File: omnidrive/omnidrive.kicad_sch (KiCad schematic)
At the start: 43 parts, among them J1 AudioJack3, J2 Conn_01x01_Pin, J3 Conn_01x01_Pin, SW1 SW_SPDT, SW2 SW_SPDT, SW3 SW_SPST, SW4 SW_SPDT, U1 TL072, U2 TL072

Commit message: annotation and ERC check
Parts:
- added C10: 0.1uF, symbol Device:C
- added C11, C8: 1uF, symbol Device:C_Polarized
- added C9: 0.047uF, symbol Device:C
- added J4, J5: Conn_01x01_Pin, symbol Connector:Conn_01x01_Pin
- added J6: AudioJack2, symbol Connector_Audio:AudioJack2
- added R18: 3.9K, symbol Device:R
- added R19: 10K, symbol Device:R
- added R20: 1K, symbol Device:R
- added RV2_Tone1: 10K, symbol Device:R_Potentiometer
- added RV3_BLEND1: 47K Log, symbol Device:R_Potentiometer
- added RV4_VOL1: 100K Log, symbol Device:R_Potentiometer
- added SW5: SW_SPST, symbol Switch:SW_SPST
- renumbered RV1 to RV1_GAIN1
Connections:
- net GND: now also C7.2, C10.1, R19.2, RV4_VOL1.3, SW5.2 (B)
- net at R17.1: now also C6.2, RV1_GAIN1.2, RV1_GAIN1.3, U2.7
- net at R17.2: now also D3.1 (K), D4.2 (A), C8.1, C9.1
- net at D4.1 (K): now also D3.2 (A), SW4.2 (B)
- net at SW4.1 (A): now also C12.1
- net at SW4.3 (C): now also C6.1, R16.1, RV1_GAIN1.1, U2.6 (-)
- net at R16.2: now also C7.1
- net at SW2.3 (C): now also C11.1
- new net: C11.2, RV3_BLEND1.3
- new net: C8.2, R18.2
- new net: C9.2, R19.1, R20.1, RV2_Tone1.3
- new net: C10.2, R18.1, RV2_Tone1.1
- new net: RV3_BLEND1.2, RV4_VOL1.1
- new net: J5.1 (Pin_1), J6.T, RV4_VOL1.2
- new net: R20.2, SW5.1 (A)
- new net: RV2_Tone1.2, RV3_BLEND1.1
- new net: J4.1 (Pin_1), J6.S

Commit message: offboarding
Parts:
- added J_BLEND_1, J_BLEND_2, J_BLEND_3, J_BOOST_1, J_BOOST_2, J_BOOST_3, J_FILT_1, J_FILT_2, J_FILT_3, J_GAIN_1, J_GAIN_2, J_GAIN_3, J_MODE_1, J_MODE_2, J_MODE_3, J_OCT_1, J_OCT_2, J_SCOOP_1, J_SCOOP_2, J_TONE_1, J_TONE_2, J_TONE_3, J_VOL_1, J_VOL_2, J_VOL_3: Conn_01x01_Pin, symbol Connector:Conn_01x01_Pin
- renumbered J2 to J_IN_SLV1, J3 to J_IN_TIP1, J4 to J_OUT_SLV1, J5 to J_OUT_TIP1, SW1 to SW_BOOST_1, SW2 to SW_FILTER_2, SW4 to SW_MODE1, SW3 to SW_OCTAVE1, SW5 to SW_SCOOP1
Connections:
- net GND: now also J1.S, J_IN_SLV1.1 (Pin_1), J_SCOOP_1.1 (Pin_1), J_VOL_1.1 (Pin_1)
- net at C11.1, SW_FILTER_2.3 (C): now also J_FILT_2.1 (Pin_1)
- net at C11.2, RV3_BLEND1.3: now also J_BLEND_1.1 (Pin_1)
- net at C6.2, R17.1, RV1_GAIN1.2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: now also J_GAIN_2.1 (Pin_1), J_GAIN_3.1 (Pin_1)
- net at R10.2, R11.2, SW_FILTER_2.2 (B): now also J_FILT_3.1 (Pin_1)
- net at D3.2 (A), D4.1 (K), SW_MODE1.2 (B): now also J_MODE_3.1 (Pin_1)
- net at C9.2, R19.1, R20.1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: now also J_TONE_2.1 (Pin_1)
- net at C10.2, R18.1, RV2_Tone1.1: now also J_TONE_1.1 (Pin_1)
- net at C1.1, R1.1, SW_BOOST_1.3 (C): now also J_BOOST_2.1 (Pin_1)
- net at RV3_BLEND1.2, RV4_VOL1.1: now also J_BLEND_2.1 (Pin_1), J_VOL_3.1 (Pin_1)
- net at J6.T, J_OUT_TIP1.1 (Pin_1), RV4_VOL1.2: now also J_VOL_2.1 (Pin_1)
- net at C12.1, SW_MODE1.1 (A): now also J_MODE_2.1 (Pin_1)
- net at C6.1, R16.1, RV1_GAIN1.1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: now also J_GAIN_1.1 (Pin_1), J_MODE_1.1 (Pin_1)
- net at D1.2 (A), R12.2, U2.2 (-): now also R11.1
- net at J1.T, J_IN_TIP1.1 (Pin_1), SW_BOOST_1.2 (B): now also J_BOOST_1.1 (Pin_1)
- net at R13.2, R14.2, SW_OCTAVE1.1 (A): now also J_OCT_2.1 (Pin_1)
- net at C2.1, R2.1, SW_BOOST_1.1 (A): now also J_BOOST_3.1 (Pin_1)
- net at R20.2, SW_SCOOP1.1 (A): now also J_SCOOP_2.1 (Pin_1)
- net at RV2_Tone1.2, RV3_BLEND1.1: now also J_BLEND_3.1 (Pin_1), J_TONE_3.1 (Pin_1)
- net at R9.1, SW_FILTER_2.1 (A), U1.7: now also J_FILT_1.1 (Pin_1)

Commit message: assigned footprints
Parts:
- C1, C2, C3, C4, C5, C6, C9: footprint (none) -> Capacitor_SMD:C_1206_3216Metric_Pad1.33x1.80mm_HandSolder
- C10: footprint (none) -> Capacitor_THT:C_Rect_L11.0mm_W6.3mm_P10.00mm_MKT
- C11, C8, J6: footprint (none) -> Capacitor_THT:CP_Radial_D6.3mm_P2.50mm
- C12, C13, C14, C7: footprint (none) -> Capacitor_THT:CP_Radial_D5.0mm_P2.50mm
- J_BLEND_1, J_BLEND_2, J_BLEND_3, J_BOOST_1, J_BOOST_2, J_BOOST_3, J_FILT_1, J_FILT_2, J_FILT_3, J_GAIN_1, J_GAIN_2, J_GAIN_3, J_IN_SLV1, J_IN_TIP1, J_MODE_1, J_MODE_2, J_MODE_3, J_OCT_1, J_OCT_2, J_OUT_SLV1, J_OUT_TIP1, J_SCOOP_1, J_SCOOP_2, J_TONE_1, J_TONE_2, J_TONE_3, J_VOL_1, J_VOL_2, J_VOL_3: footprint (none) -> Connector_PinHeader_1.00mm:PinHeader_1x01_P1.00mm_Vertical
- R1, R10, R11, R12, R13, R14, R15, R16, R17, R18, R19, R2, R20, R21, R22, R3, R4, R5, R6, R7, R8, R9, U1, U2: footprint (none) -> Resistor_SMD:R_1206_3216Metric_Pad1.30x1.75mm_HandSolder

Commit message: start placement
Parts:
- added BT1: 9V, symbol Device:Battery_Cell
- added J_BATT_NEG1, J_BATT_POS1: Conn_01x01_Pin, Connector_PinHeader_1.00mm:PinHeader_1x01_P1.00mm_Vertical, symbol Connector:Conn_01x01_Pin
- U1, U2: footprint Resistor_SMD:R_1206_3216Metric_Pad1.30x1.75mm_HandSolder -> Package_DIP:DIP-8_W7.62mm
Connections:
- net +9V: now also BT1.1 (+), J_BATT_POS1.1 (Pin_1)
- net at J1.R: now also BT1.2 (-), J_BATT_NEG1.1 (Pin_1)
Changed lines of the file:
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@@
   (junction (at 67.31 25.4) (diameter 0) (color 0 0 0 0)
   )
+  (junction (at 35.56 67.31) (diameter 0) (color 0 0 0 0)
+  )
+  (junction (at 60.96 63.5) (diameter 0) (color 0 0 0 0)
+  )
   (junction (at 97.79 77.47) (diameter 0) (color 0 0 0 0)
   )
@@
   (junction (at 76.2 77.47) (diameter 0) (color 0 0 0 0)
   )
+  (junction (at 22.86 48.26) (diameter 0) (color 0 0 0 0)
+  )
   (junction (at 191.77 114.3) (diameter 0) (color 0 0 0 0)
   )
@@
   (junction (at 135.89 36.83) (diameter 0) (color 0 0 0 0)
   )
+  (junction (at 35.56 58.42) (diameter 0) (color 0 0 0 0)
+  )
   (junction (at 64.77 63.5) (diameter 0) (color 0 0 0 0)
   )
@@
     (stroke (width 0) (type default))
   )
+  (wire (pts (xy 45.72 58.42) (xy 60.96 58.42))
+    (stroke (width 0) (type default))
+  )
   (wire (pts (xy 170.18 53.34) (xy 170.18 55.88))
     (stroke (width 0) (type default))
@@
     (stroke (width 0) (type default))
   )
+  (wire (pts (xy 20.32 58.42) (xy 35.56 58.42))
+    (stroke (width 0) (type default))
+  )
   (wire (pts (xy 255.27 16.51) (xy 255.27 67.31))
     (stroke (width 0) (type default))
@@
     (stroke (width 0) (type default))
   )
+  (wire (pts (xy 31.75 33.02) (xy 31.75 40.64))
+    (stroke (width 0) (type default))
+  )
   (wire (pts (xy 128.27 101.6) (xy 128.27 67.31))
     (stroke (width 0) (type default))
@@
     (stroke (width 0) (type default))
   )
+  (wire (pts (xy 60.96 58.42) (xy 60.96 63.5))
+    (stroke (width 0) (type default))
+  )
   (wire (pts (xy 208.28 35.56) (xy 204.47 35.56))
     (stroke (width 0) (type default))
@@
     (stroke (width 0) (type default))
   )
+  (wire (pts (xy 31.75 40.64) (xy 22.86 40.64))
+    (stroke (width 0) (type default))
+  )
   (wire (pts (xy 191.77 99.06) (xy 191.77 101.6))
     (stroke (width 0) (type default))
   )
-  (wire (pts (xy 55.88 63.5) (xy 64.77 63.5))
+  (wire (pts (xy 55.88 63.5) (xy 60.96 63.5))
     (stroke (width 0) (type default))
   )
@@
     (stroke (width 0) (type default))
   )
+  (wire (pts (xy 22.86 48.26) (xy 20.32 48.26))
+    (stroke (width 0) (type default))
+  )
   (wire (pts (xy 80.01 36.83) (xy 85.09 36.83))
     (stroke (width 0) (type default))
@@
     (stroke (width 0) (type default))
   )
+  (wire (pts (xy 35.56 67.31) (xy 45.72 67.31))
+    (stroke (width 0) (type default))
+  )
   (wire (pts (xy 148.59 36.83) (xy 156.21 36.83))
     (stroke (width 0) (type default))
@@
     (stroke (width 0) (type default))
   )
+  (wire (pts (xy 35.56 58.42) (xy 35.56 67.31))
+    (stroke (width 0) (type default))
+  )
   (wire (pts (xy 144.78 93.98) (xy 144.78 101.6))
     (stroke (width 0) (type default))
@@
     (stroke (width 0) (type default))
   )
+  (wire (pts (xy 22.86 40.64) (xy 22.86 48.26))
+    (stroke (width 0) (type default))
+  )
   (wire (pts (xy 134.62 20.32) (xy 142.24 20.32))
     (stroke (width 0) (type default))
@@
     (stroke (width 0) (type default))
   )
+  (wire (pts (xy 60.96 63.5) (xy 64.77 63.5))
+    (stroke (width 0) (type default))
+  )
   (wire (pts (xy 187.96 97.79) (xy 187.96 99.06))
     (stroke (width 0) (type default))
@@
     (stroke (width 0) (type default))
   )
+  (wire (pts (xy 45.72 67.31) (xy 45.72 58.42))
+    (stroke (width 0) (type default))
+  )
   (wire (pts (xy 154.94 58.42) (xy 76.2 58.42))
     (stroke (width 0) (type default))
@@
     (stroke (width 0) (type default))
   )
+  (wire (pts (xy 26.67 33.02) (xy 31.75 33.02))
+    (stroke (width 0) (type default))
+  )
   (wire (pts (xy 237.49 25.4) (xy 237.49 30.48))
     (stroke (width 0) (type default))
@@
     (stroke (width 0) (type default))
   )
+  (wire (pts (xy 35.56 58.42) (xy 36.83 58.42))
+    (stroke (width 0) (type default))
+  )
   (wire (pts (xy 64.77 30.48) (xy 69.85 30.48))
     (stroke (width 0) (type default))
@@
     (stroke (width 0) (type default))
   )
+  (wire (pts (xy 20.32 48.26) (xy 20.32 50.8))
+    (stroke (width 0) (type default))
+  )
   (wire (pts (xy 53.34 29.21) (xy 53.34 27.94))
     (stroke (width 0) (type default))
@@
     )
   )
+  (symbol (lib_id "Connector:Conn_01x01_Pin") (at 27.94 48.26 0) (mirror y) (unit 1)
+    (in_bom yes) (on_board yes) (dnp no)
+    (property "Reference" "J_BATT_NEG1" (at 27.305 43.18 0)
+      (effects (font (size 1.27 1.27)))
+    )
+    (property "Value" "Conn_01x01_Pin" (at 27.305 45.72 0)
+      (effects (font (size 1.27 1.27)))
+    )
+    (property "Footprint" "Connector_PinHeader_1.00mm:PinHeader_1x01_P1.00mm_Vertical" (at 27.94 48.26 0)
+      (effects (font (size 1.27 1.27)) hide)
+    )
+    (property "Datasheet" "~" (at 27.94 48.26 0)
+      (effects (font (size 1.27 1.27)) hide)
+    )
+    (pin "1")
+    (instances
+      (project "omnidrive"
+        (path "/2afaead6-7d3e-4c2a-adc8-ba736ff6308b"
+          (reference "J_BATT_NEG1") (unit 1)
+        )
+      )
+    )
+  )
   (symbol (lib_id "power:GND") (at 161.29 114.3 0) (unit 1)
     (in_bom yes) (on_board yes) (dnp no) (fields_autoplaced)
@@
       (effects (font (size 1.27 1.27)))
     )
-    (property "Footprint" "Resistor_SMD:R_1206_3216Metric_Pad1.30x1.75mm_HandSolder" (at 214.63 53.34 0)
+    (property "Footprint" "Package_DIP:DIP-8_W7.62mm" (at 214.63 53.34 0)
       (effects (font (size 1.27 1.27)) hide)
     )
@@
       (effects (font (size 1.27 1.27)))
     )
-    (property "Footprint" "Resistor_SMD:R_1206_3216Metric_Pad1.30x1.75mm_HandSolder" (at 218.44 60.96 0)
+    (property "Footprint" "Package_DIP:DIP-8_W7.62mm" (at 218.44 60.96 0)
       (effects (font (size 1.27 1.27)) hide)
     )
@@
     )
   )
+  (symbol (lib_id "Device:Battery_Cell") (at 20.32 53.34 0) (mirror x) (unit 1)
+    (in_bom yes) (on_board no) (dnp no)
+    (property "Reference" "BT1" (at 24.13 56.4515 0)
+      (effects (font (size 1.27 1.27)) (justify left))
+    )
+    (property "Value" "9V" (at 24.13 53.9115 0)
+      (effects (font (size 1.27 1.27)) (justify left))
+    )
+    (property "Footprint" "" (at 20.32 54.864 90)
+      (effects (font (size 1.27 1.27)) hide)
+    )
+    (property "Datasheet" "~" (at 20.32 54.864 90)
+      (effects (font (size 1.27 1.27)) hide)
+    )
+    (pin "1")
+    (pin "2")
+    (instances
+      (project "omnidrive"
+        (path "/2afaead6-7d3e-4c2a-adc8-ba736ff6308b"
+          (reference "BT1") (unit 1)
+        )
+      )
+    )
+  )
   (symbol (lib_id "Amplifier_Operational:TL072") (at 106.68 33.02 0) (mirror x) (unit 1)
     (in_bom yes) (on_board yes) (dnp no) (fields_autoplaced)
@@
       (effects (font (size 1.27 1.27)))
     )
-    (property "Footprint" "Resistor_SMD:R_1206_3216Metric_Pad1.30x1.75mm_HandSolder" (at 106.68 33.02 0)
+    (property "Footprint" "Package_DIP:DIP-8_W7.62mm" (at 106.68 33.02 0)
       (effects (font (size 1.27 1.27)) hide)
     )
@@
   )
   (symbol (lib_id "Connector_Audio:AudioJack2") (at 234.95 107.95 0) (mirror y) (unit 1)
-    (in_bom yes) (on_board yes) (dnp no) (fields_autoplaced)
+    (in_bom yes) (on_board no) (dnp no) (fields_autoplaced)
     (property "Reference" "J6" (at 240.03 106.045 0)
       (effects (font (size 1.27 1.27)) (justify right))
@@
       (effects (font (size 1.27 1.27)))
     )
-    (property "Footprint" "Resistor_SMD:R_1206_3216Metric_Pad1.30x1.75mm_HandSolder" (at 86.36 67.31 0)
+    (property "Footprint" "Package_DIP:DIP-8_W7.62mm" (at 86.36 67.31 0)
       (effects (font (size 1.27 1.27)) hide)
     )
@@
       (effects (font (size 1.27 1.27)))
     )
-    (property "Footprint" "Resistor_SMD:R_1206_3216Metric_Pad1.30x1.75mm_HandSolder" (at 105.41 46.99 0)
+    (property "Footprint" "Package_DIP:DIP-8_W7.62mm" (at 105.41 46.99 0)
       (effects (font (size 1.27 1.27)) hide)
     )
@@
       (effects (font (size 1.27 1.27)))
     )
-    (property "Footprint" "Resistor_SMD:R_1206_3216Metric_Pad1.30x1.75mm_HandSolder" (at 163.83 27.94 0)
+    (property "Footprint" "Package_DIP:DIP-8_W7.62mm" (at 163.83 27.94 0)
       (effects (font (size 1.27 1.27)) hide)
     )
@@
         )
       )
+    )
+  )
+  (symbol (lib_id "Connector:Conn_01x01_Pin") (at 30.48 67.31 0) (unit 1)
+    (in_bom yes) (on_board yes) (dnp no) (fields_autoplaced)
+    (property "Reference" "J_BATT_POS1" (at 31.115 62.23 0)
+      (effects (font (size 1.27 1.27)))
+    )
+    (property "Value" "Conn_01x01_Pin" (at 31.115 64.77 0)
+      (effects (font (size 1.27 1.27)))
+    )
+    (property "Footprint" "Connector_PinHeader_1.00mm:PinHeader_1x01_P1.00mm_Vertical" (at 30.48 67.31 0)
+      (effects (font (size 1.27 1.27)) hide)
+    )
+    (property "Datasheet" "~" (at 30.48 67.31 0)
+      (effects (font (size 1.27 1.27)) hide)
+    )
+    (pin "1")
+    (instances
+      (project "omnidrive"
+        (path "/2afaead6-7d3e-4c2a-adc8-ba736ff6308b"
+          (reference "J_BATT_POS1") (unit 1)
+        )
+      )

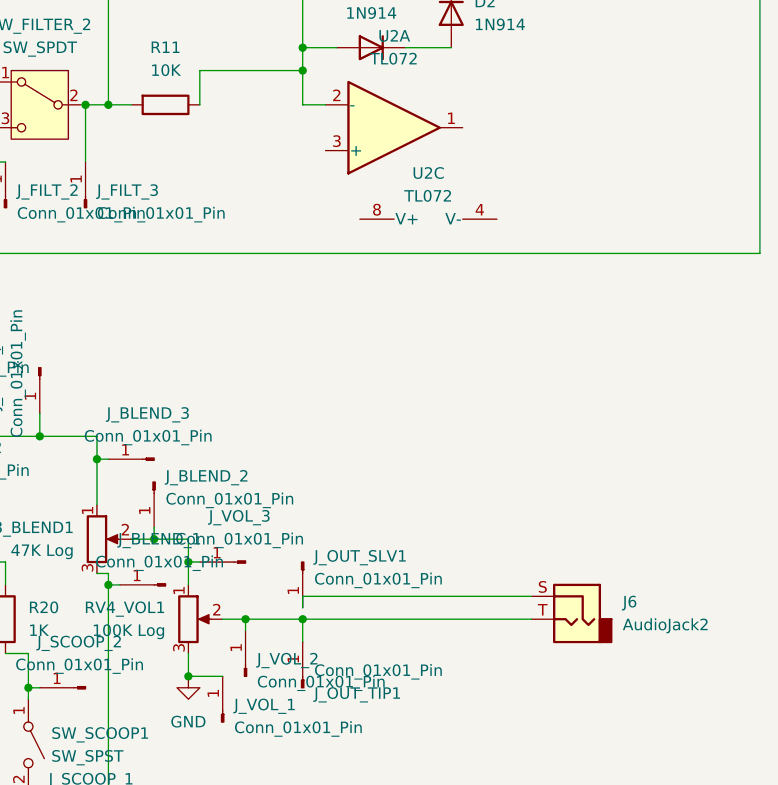
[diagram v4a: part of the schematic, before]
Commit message: more placement, attach output jack
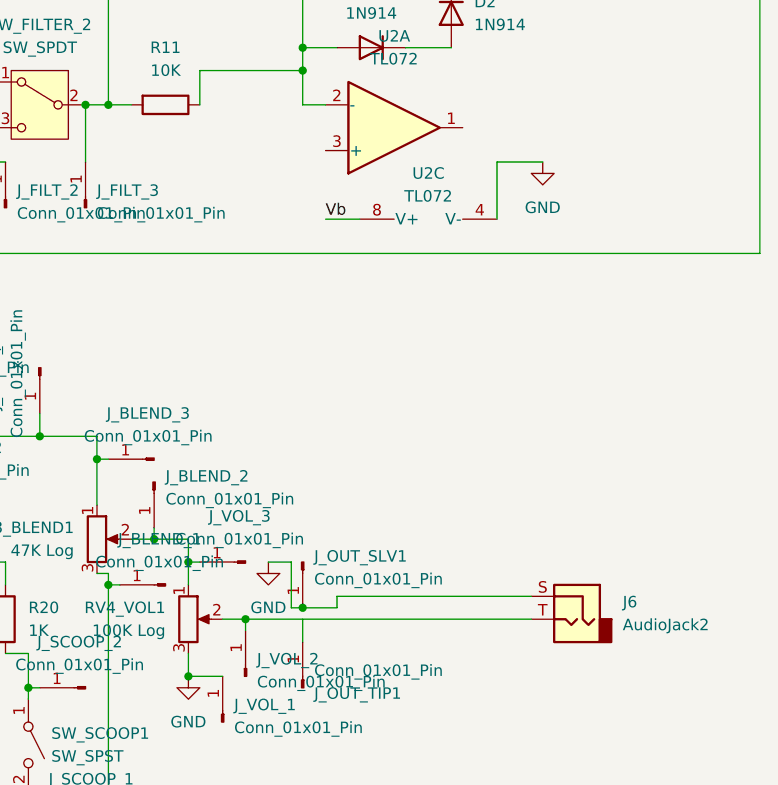
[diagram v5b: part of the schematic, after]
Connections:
- net GND: now also J6.S, J_OUT_SLV1.1 (Pin_1), U2.4 (V-)
- net Vb: now also U2.8 (V+)
- net at J6.T, J_VOL_2.1 (Pin_1), RV4_VOL1.2: no longer J_OUT_TIP1.1 (Pin_1)
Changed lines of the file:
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@@
   (junction (at 204.47 46.99) (diameter 0) (color 0 0 0 0)
   )
-  (junction (at 204.47 107.95) (diameter 0) (color 0 0 0 0)
-  )
   (junction (at 182.88 50.8) (diameter 0) (color 0 0 0 0)
   )
@@
   (junction (at 116.84 104.14) (diameter 0) (color 0 0 0 0)
   )
+  (junction (at 204.47 106.68) (diameter 0) (color 0 0 0 0)
+  )
   (junction (at 49.53 34.29) (diameter 0) (color 0 0 0 0)
   )
@@
     (stroke (width 0) (type default))
   )
+  (wire (pts (xy 207.01 63.5) (xy 210.82 63.5))
+    (stroke (width 0) (type default))
+  )
+  (wire (pts (xy 226.06 57.15) (xy 226.06 63.5))
+    (stroke (width 0) (type default))
+  )
   (wire (pts (xy 49.53 39.37) (xy 49.53 34.29))
     (stroke (width 0) (type default))
@@
     (stroke (width 0) (type default))
   )
+  (wire (pts (xy 208.28 105.41) (xy 208.28 106.68))
+    (stroke (width 0) (type default))
+  )
   (wire (pts (xy 170.18 53.34) (xy 170.18 55.88))
     (stroke (width 0) (type default))
@@
     (stroke (width 0) (type default))
   )
+  (wire (pts (xy 208.28 106.68) (xy 204.47 106.68))
+    (stroke (width 0) (type default))
+  )
   (wire (pts (xy 100.33 20.32) (xy 96.52 20.32))
     (stroke (width 0) (type default))
@@
     (stroke (width 0) (type default))
   )
-  (wire (pts (xy 229.87 105.41) (xy 204.47 105.41))
+  (wire (pts (xy 229.87 105.41) (xy 208.28 105.41))
     (stroke (width 0) (type default))
   )
@@
     (stroke (width 0) (type default))
   )
-  (wire (pts (xy 229.87 107.95) (xy 204.47 107.95))
-    (stroke (width 0) (type default))
-  )
   (wire (pts (xy 161.29 91.44) (xy 161.29 93.98))
     (stroke (width 0) (type default))
@@
     (stroke (width 0) (type default))
   )
+  (wire (pts (xy 203.2 101.6) (xy 203.2 106.68))
+    (stroke (width 0) (type default))
+  )
   (wire (pts (xy 76.2 77.47) (xy 76.2 92.71))
     (stroke (width 0) (type default))
@@
     (stroke (width 0) (type default))
   )
-  (wire (pts (xy 204.47 105.41) (xy 204.47 106.68))
-    (stroke (width 0) (type default))
-  )
   (wire (pts (xy 64.77 73.66) (xy 64.77 74.93))
     (stroke (width 0) (type default))
@@
     (stroke (width 0) (type default))
   )
+  (wire (pts (xy 200.66 101.6) (xy 203.2 101.6))
+    (stroke (width 0) (type default))
+  )
   (wire (pts (xy 93.98 25.4) (xy 93.98 30.48))
     (stroke (width 0) (type default))
@@
     (stroke (width 0) (type default))
   )
+  (wire (pts (xy 231.14 57.15) (xy 226.06 57.15))
+    (stroke (width 0) (type default))
+  )
   (wire (pts (xy 142.24 20.32) (xy 143.51 20.32))
     (stroke (width 0) (type default))
@@
     (stroke (width 0) (type default))
   )
-  (wire (pts (xy 198.12 107.95) (xy 204.47 107.95))
+  (wire (pts (xy 198.12 107.95) (xy 229.87 107.95))
     (stroke (width 0) (type default))
   )
@@
   )
   (wire (pts (xy 173.99 115.57) (xy 173.99 116.84))
+    (stroke (width 0) (type default))
+  )
+  (wire (pts (xy 203.2 106.68) (xy 204.47 106.68))
     (stroke (width 0) (type default))
   )
@@
   )
   (label "Vb" (at 97.79 38.1 0) (fields_autoplaced)
+    (effects (font (size 1.27 1.27)) (justify left bottom))
+  )
+  (label "Vb" (at 207.01 63.5 0) (fields_autoplaced)
     (effects (font (size 1.27 1.27)) (justify left bottom))
   )
@@
     )
   )
+  (symbol (lib_id "power:GND") (at 231.14 57.15 0) (unit 1)
+    (in_bom yes) (on_board yes) (dnp no) (fields_autoplaced)
+    (property "Reference" "#PWR016" (at 231.14 63.5 0)
+      (effects (font (size 1.27 1.27)) hide)
+    )
+    (property "Value" "GND" (at 231.14 62.23 0)
+      (effects (font (size 1.27 1.27)))
+    )
+    (property "Footprint" "" (at 231.14 57.15 0)
+      (effects (font (size 1.27 1.27)) hide)
+    )
+    (property "Datasheet" "" (at 231.14 57.15 0)
+      (effects (font (size 1.27 1.27)) hide)
+    )
+    (pin "1")
+    (instances
+      (project "omnidrive"
+        (path "/2afaead6-7d3e-4c2a-adc8-ba736ff6308b"
+          (reference "#PWR016") (unit 1)
+        )
+      )
+    )
+  )
   (symbol (lib_id "Diode:1N914") (at 121.92 76.2 90) (mirror x) (unit 1)
     (in_bom yes) (on_board yes) (dnp no) (fields_autoplaced)
@@
         )
       )
+    )
+  )
+  (symbol (lib_id "power:GND") (at 200.66 101.6 0) (unit 1)
+    (in_bom yes) (on_board yes) (dnp no) (fields_autoplaced)
+    (property "Reference" "#PWR017" (at 200.66 107.95 0)
+      (effects (font (size 1.27 1.27)) hide)
+    )
+    (property "Value" "GND" (at 200.66 106.68 0)
+      (effects (font (size 1.27 1.27)))
+    )
+    (property "Footprint" "" (at 200.66 101.6 0)
+      (effects (font (size 1.27 1.27)) hide)
+    )
+    (property "Datasheet" "" (at 200.66 101.6 0)
+      (effects (font (size 1.27 1.27)) hide)
+    )
+    (pin "1")
+    (instances
+      (project "omnidrive"
+        (path "/2afaead6-7d3e-4c2a-adc8-ba736ff6308b"
+          (reference "#PWR017") (unit 1)
+        )
+      )
